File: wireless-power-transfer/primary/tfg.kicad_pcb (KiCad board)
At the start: 2 copper layers, 160 x 100 mm, 57 parts, among them J1 CONN_01X06, J2 Screw_Terminal_1x02, J3 BARREL_JACK, Q1 IRLB8721PBF, Q2 IRLB8721PBF, Q3 IRLB8721PBF, Q4 IRLB8721PBF, U1 PIC18F45K20-I/PT, U2 IR2110, U3 IR2110, U4 R-78E15, U5 R-78E3.3, U6 XBEE_Wi-Fi

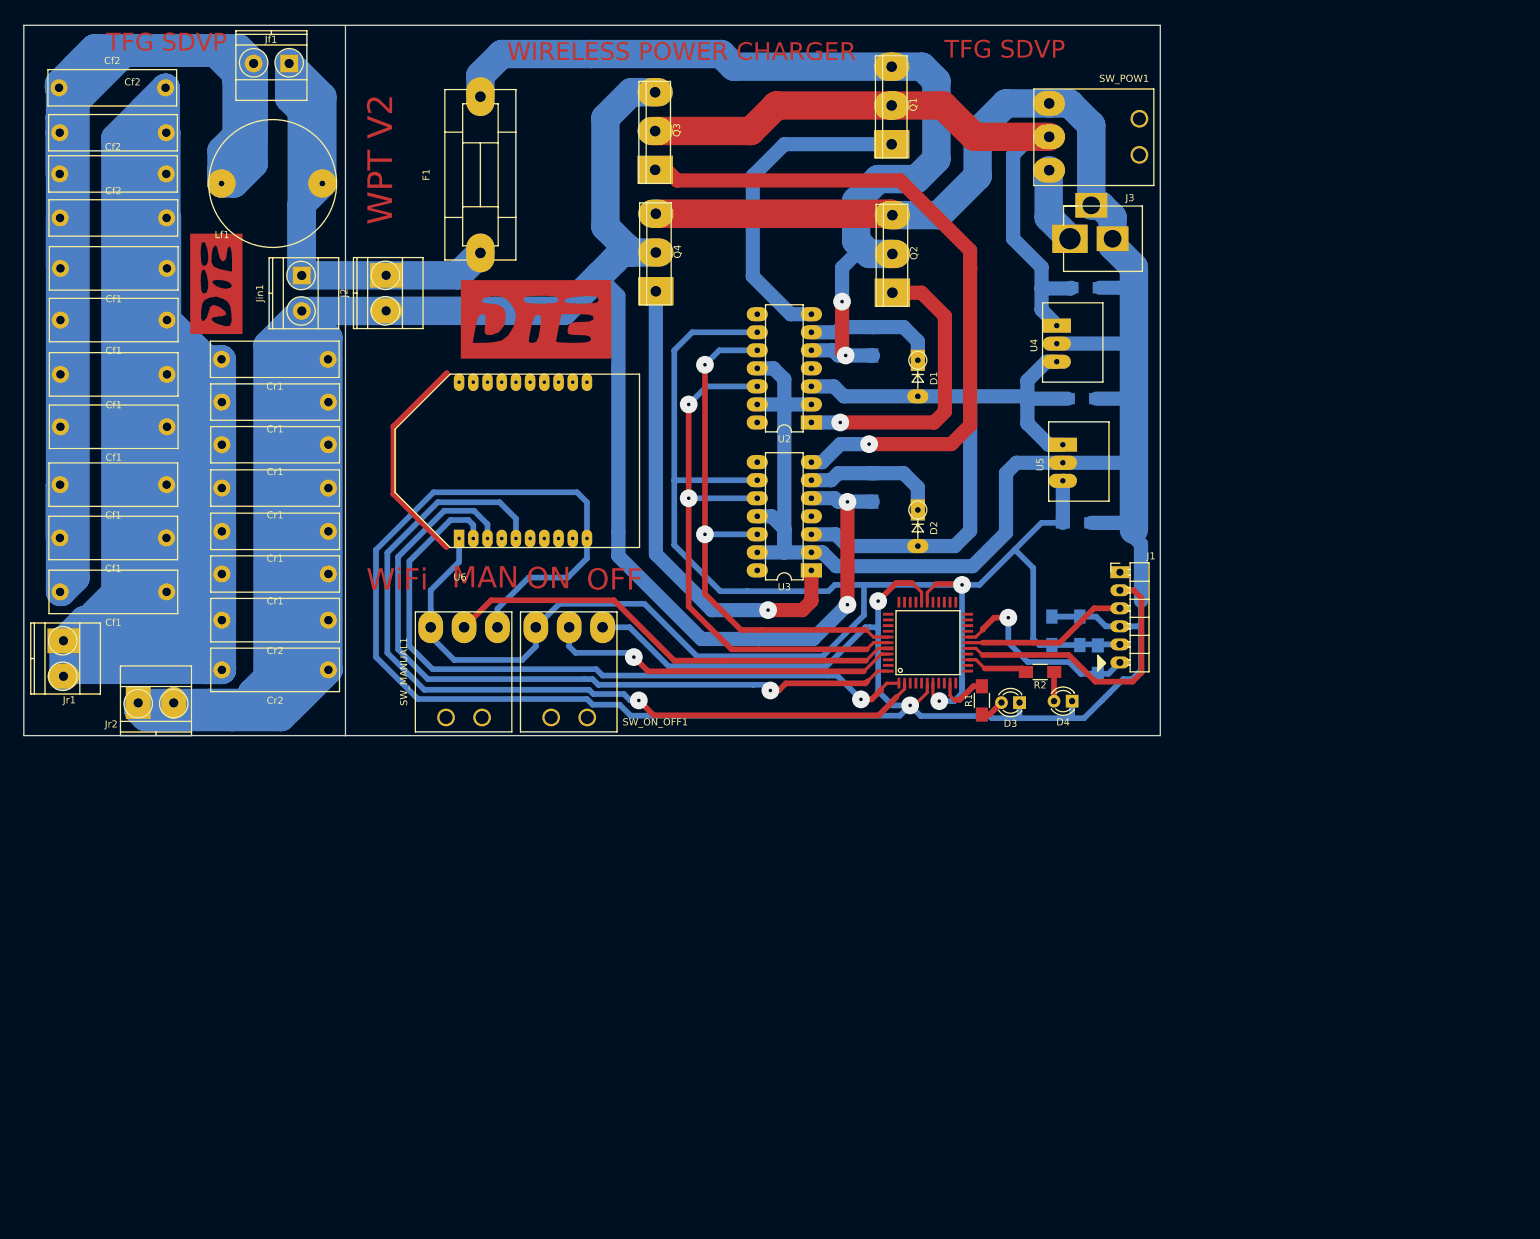
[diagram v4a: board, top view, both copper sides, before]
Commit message: Prepare Silk Layer in order to be able to manufacture
This 'manu2' branch was created in order to have the 3 projects
on the same folder.

The silk layer was created and adapted to give it to an external
manufacturer.
Nearly the same information was created in the copper layer in order to
have this information also in the case the PCB's were manufactured in
the DTE.
The Mask layer was also adapted to give it to the external manufacturer.
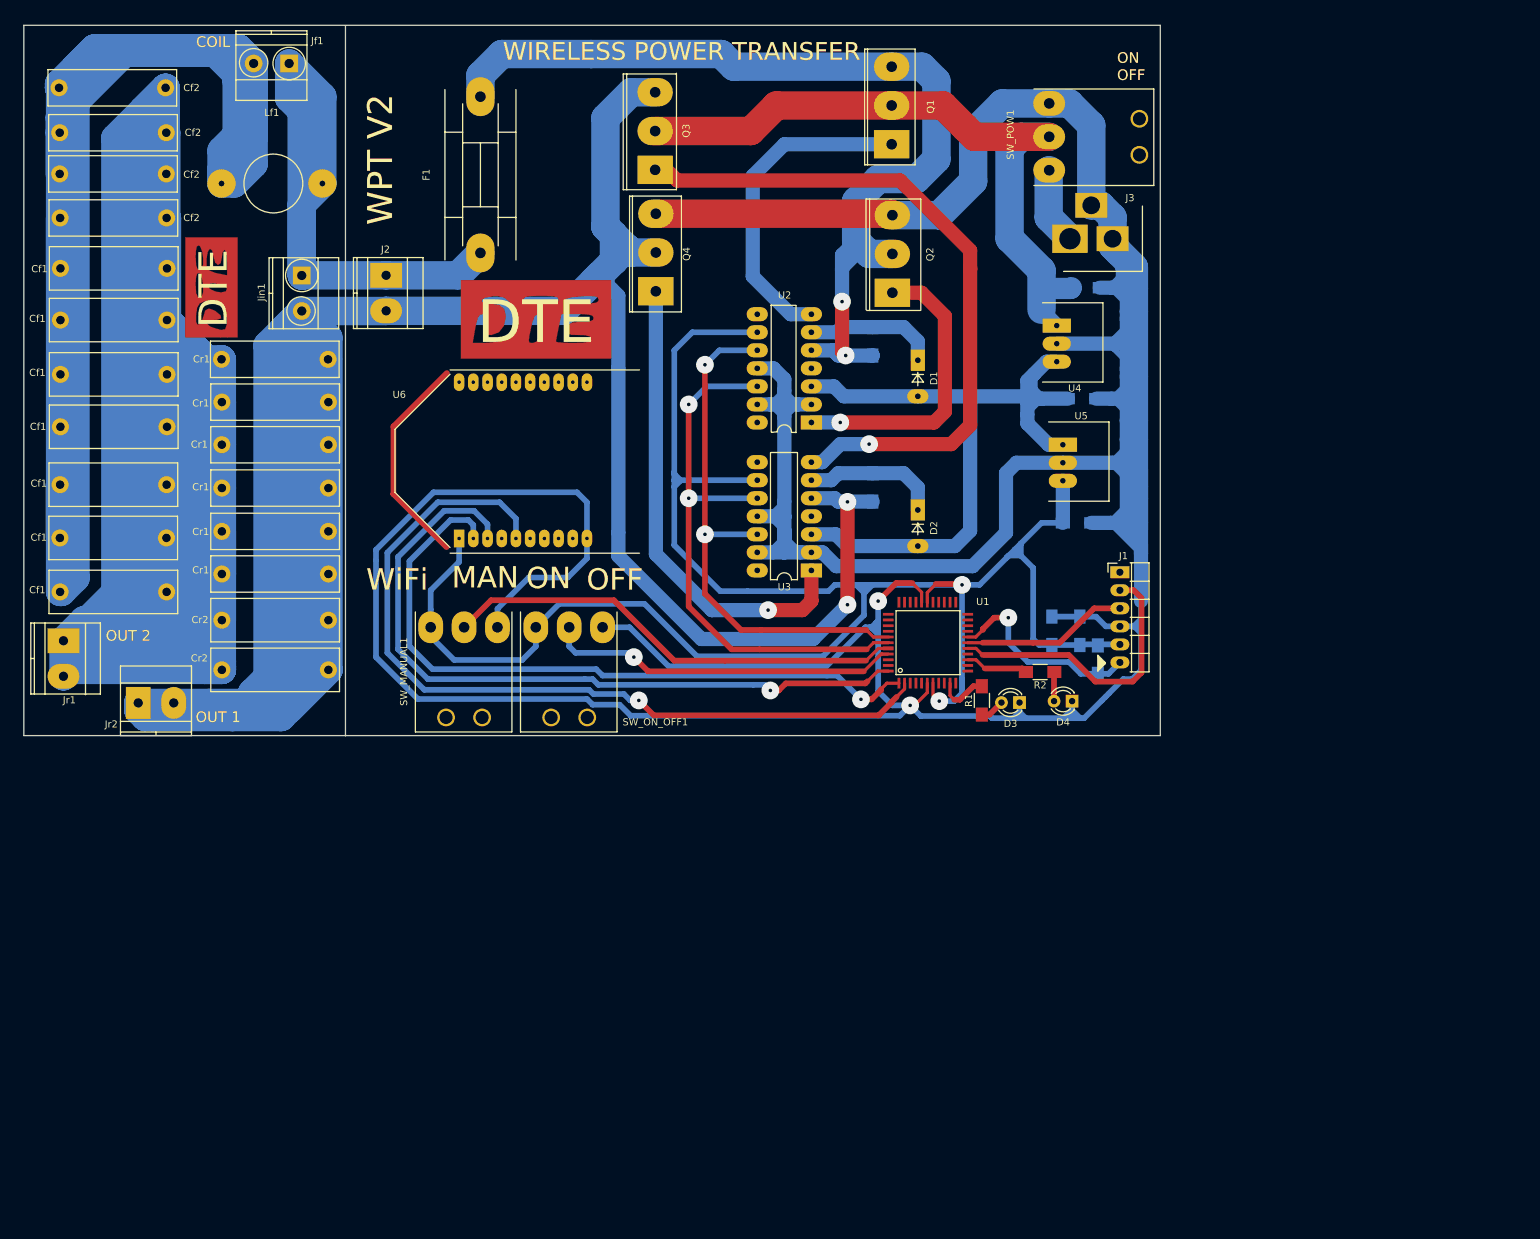
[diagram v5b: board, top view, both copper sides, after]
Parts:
- moved G*** 0.86 mm to (84.3, 62.5)
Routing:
- net Net-(C1-Pad2): track 582.4 -> 690.2 mm
- net Net-(C5-Pad1): track 95.8 -> 137.7 mm
- net Carga0: track 505.7 -> 519.3 mm
- net /+15V: track 98.8 -> 109.4 mm
- net /+3.3V: track 266.7 -> 276.5 mm
- net Net-(Cboot1-Pad2): track 136.0 -> 141.0 mm
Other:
- rule pad_to_mask_clearance: 0.2 -> 0.1
- board text added: "COIL"
- board text added: "DTE"
- board text added: "ON OFF"
- board text added: "OUT 1"
- board text added: "OUT 2"
- board text added: "WIRELESS POWER TRANSFER"
- board text removed: "TFG SDVP"
- board text removed: "WIRELESS POWER CHARGER"

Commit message: PDFs created with schematics and PCB layers for front and back sides.
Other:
- board text added: "3/7"
- board text removed: "DTE"
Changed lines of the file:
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@@
-(kicad_pcb (version 4) (host pcbnew 4.0.0-rc2-stable)
+(kicad_pcb (version 4) (host pcbnew 4.0.6)
   (general
     (links 127)
     (no_connects 13)
-    (area 57.819999 25.526999 223.280001 126.325001)
+    (area 57.819999 25.526999 268.528572 193.85)
     (thickness 1.6)
-    (drawings 54)
+    (drawings 53)
     (tracks 800)
     (zones 0)
@@
     (visible_elements 7FFEFF79)
     (pcbplotparams
-      (layerselection 0x010e0_80000001)
-      (usegerberextensions true)
+      (layerselection 0x01020_00000001)
+      (usegerberextensions false)
       (excludeedgelayer true)
       (linewidth 0.100000)
@@
       (padsonsilk false)
       (subtractmaskfromsilk false)
-      (outputformat 1)
+      (outputformat 4)
       (mirror false)
-      (drillshape 0)
+      (drillshape 2)
       (scaleselection 1)
-      (outputdirectory C:/GIT/GERBER/wpt-primary/))
+      (outputdirectory ""))
   )
   (net 0 "")
@@
     )
   )
+  (gr_text 3/7 (at 264.1 191.3) (layer F.Cu)
+    (effects (font (size 3 3) (thickness 0.3)))
+  )
   (gr_text "ON\nOFF\n" (at 211.8 31.4) (layer F.SilkS)
     (effects (font (size 1.5 1.5) (thickness 0.3)) (justify left))
@@
     (effects (font (size 1.5 1.5) (thickness 0.3)))
   )
-  (gr_text DTE (at 130 67.4) (layer F.SilkS)
-    (effects (font (size 6 6) (thickness 0.8)))
-  )
-  (gr_text DTE (at 84.6 62.65 90) (layer F.SilkS)
-    (effects (font (size 4 4) (thickness 0.8)))
-  )
   (gr_text OFF (at 141.1 103.65) (layer F.SilkS)
